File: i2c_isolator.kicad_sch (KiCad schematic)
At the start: 6 parts, among them U8 TS5A23157RSER

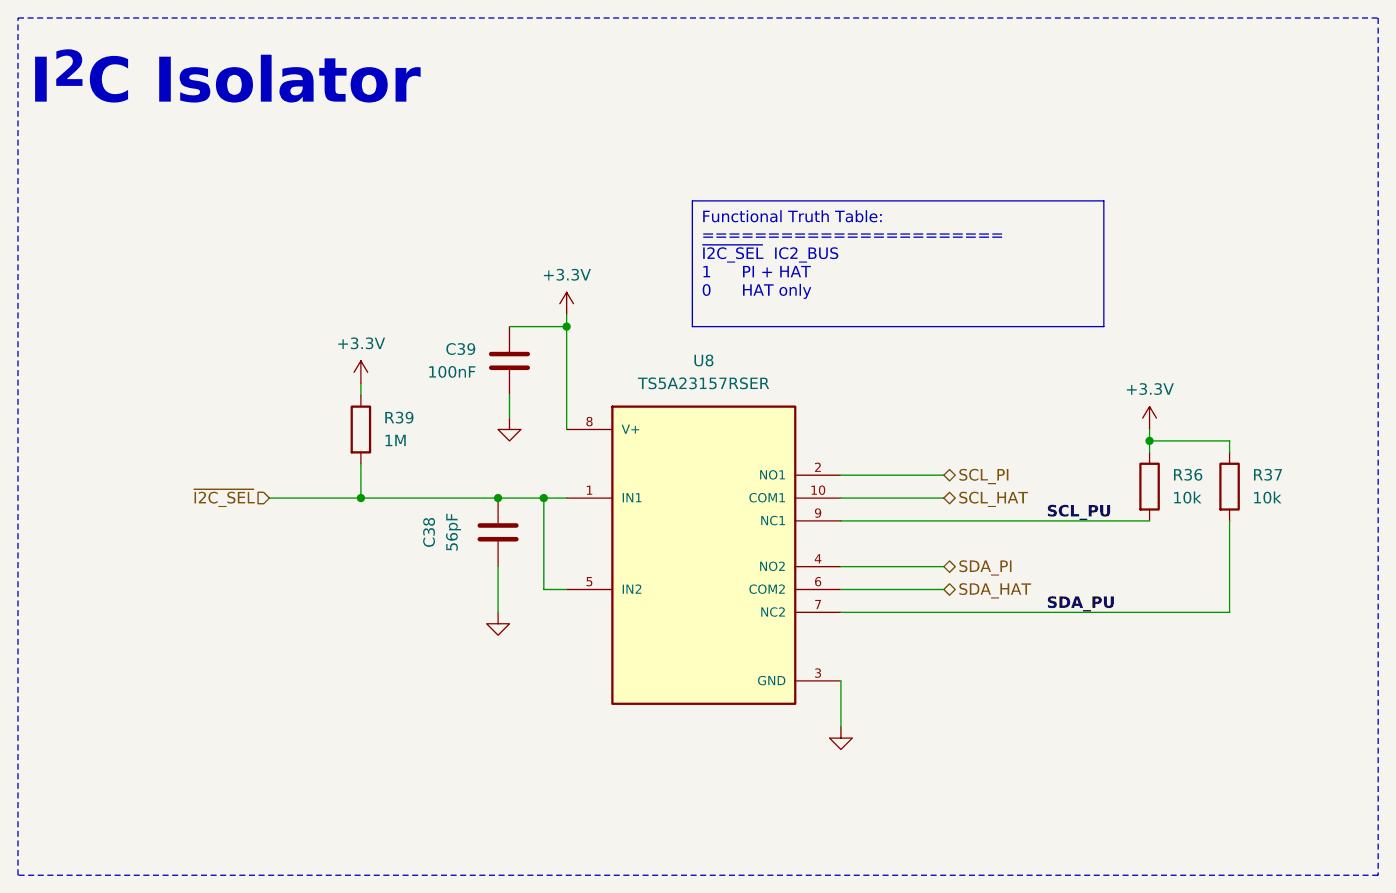
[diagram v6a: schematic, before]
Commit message: feat: 3V3 regulator + complete rework to 16 layers
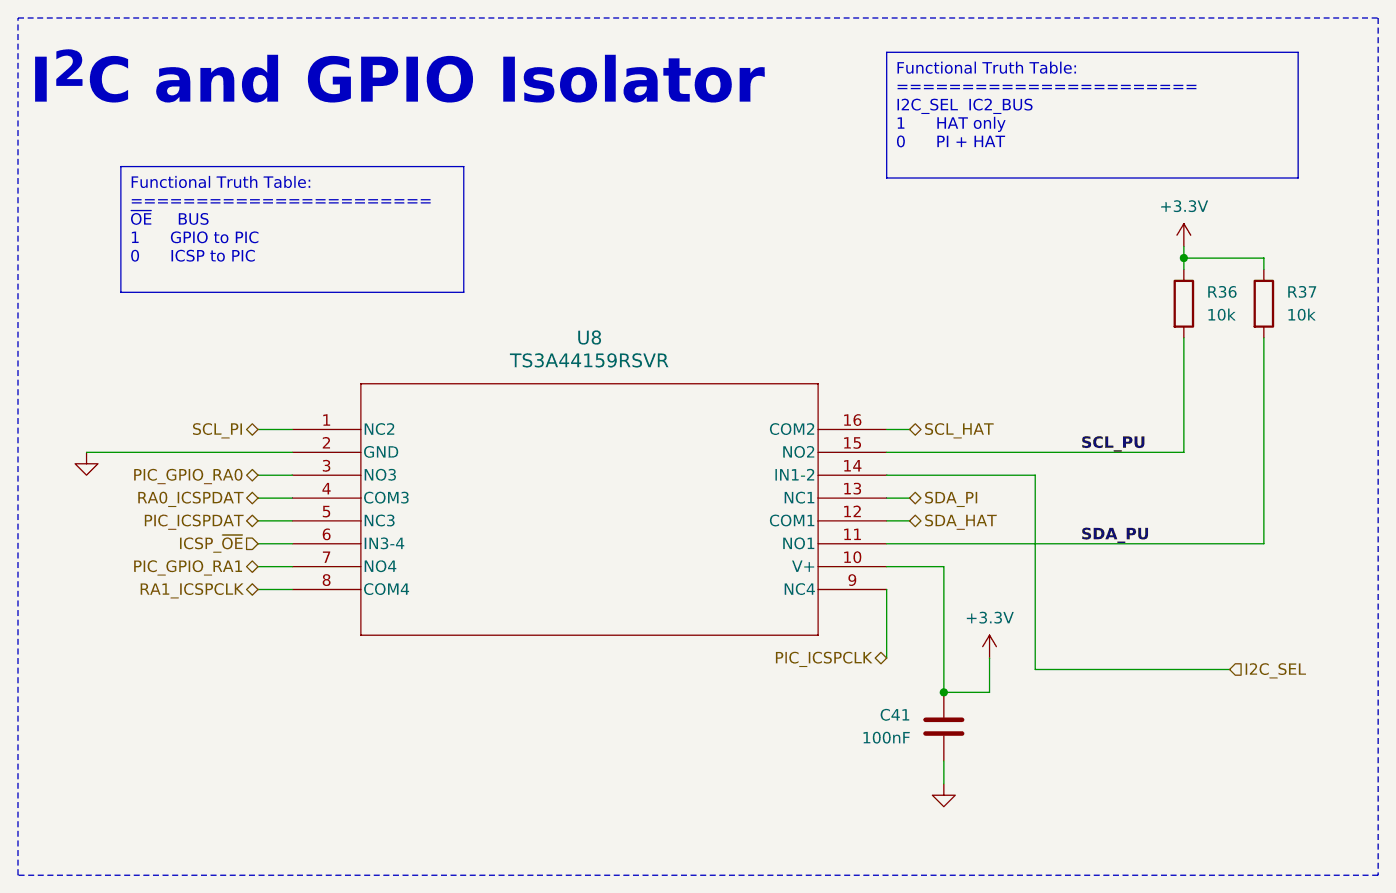
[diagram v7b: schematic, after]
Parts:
- removed C38: 56pF, Capacitor_SMD:C_0402_1005Metric, symbol Device:C
- removed C39: 100nF, Capacitor_SMD:C_0402_1005Metric, symbol Device:C
- removed R39: 1M, Resistor_SMD:R_0402_1005Metric, symbol Device:R
- removed U8: TS5A23157RSER, effectiveRangeHat:IC_TS5A23157RSER, symbol effectiveRangeHat_kicad_sym:TS5A23157RSER
- added C41: 100nF, Capacitor_SMD:C_0402_1005Metric, symbol Device:C
- added U8: TS3A44159RSVR, effectiveRangeHat:RSV16, symbol effectiveRangeHat_kicad_sym:TS3A44159RSVR
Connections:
- net +3.3V: now also C41.2, U8.10 (V+)
- net GND: now also C41.1, U8.2 (GND)
- net SCL_HAT: now also U8.16 (COM2)
- net SCL_PI: now also U8.1 (NC2)
- net SCL_PU: now also U8.15 (NO2)
- net SDA_HAT: now also U8.12 (COM1)
- net SDA_PI: now also U8.13 (NC1)
- net SDA_PU: now also U8.11 (NO1)
- new net I2C_SEL: U8.14 (IN1-2)
- new net ICSP_~{OE}: U8.6 (IN3-4)
- new net PIC_GPIO_RA0: U8.3 (NO3)
- new net PIC_GPIO_RA1: U8.7 (NO4)
- new net PIC_ICSPCLK: U8.9 (NC4)
- new net PIC_ICSPDAT: U8.5 (NC3)
- new net RA0_ICSPDAT: U8.4 (COM3)
- new net RA1_ICSPCLK: U8.8 (COM4)
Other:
- note added: "I^{2}C and GPIO Isolator"
- note removed: "I^{2}C Isolator"
- moved on the sheet: R36, R37
